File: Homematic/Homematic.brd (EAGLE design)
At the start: 99.2 x 85 mm, 26 parts, among them IC1 3.3V, IC2 3.3V, P1 DF11-06-2DS, Q1 BS170

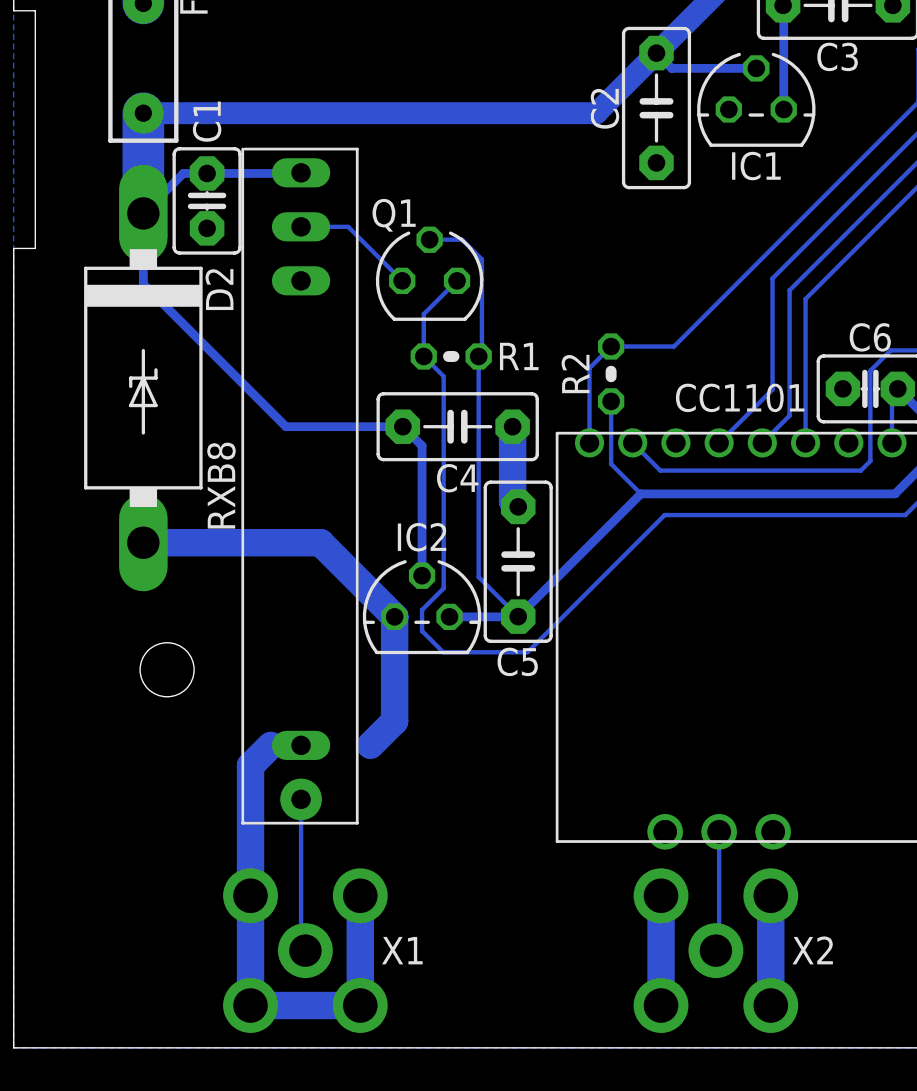
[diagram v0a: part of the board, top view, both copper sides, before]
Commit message: Fix RXB8 package. Add low pass filter.
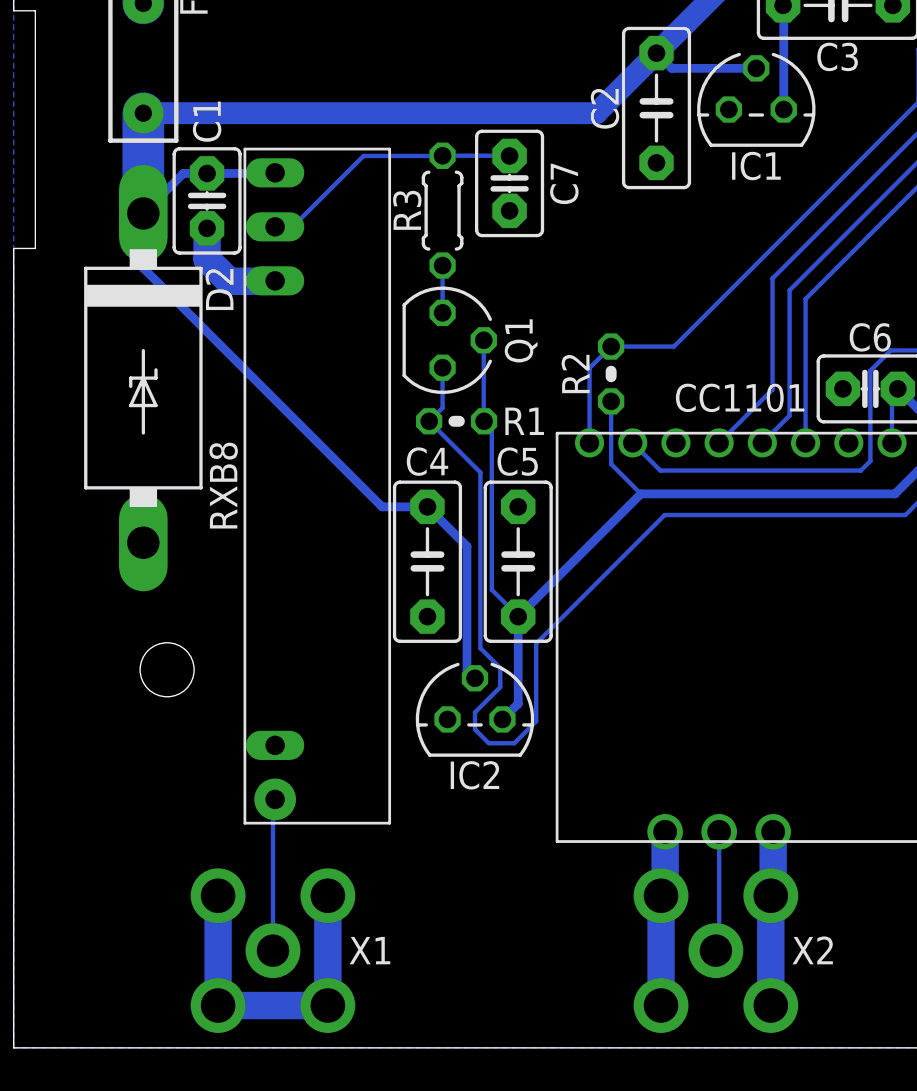
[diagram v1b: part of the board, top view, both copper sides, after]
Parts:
- added C7: 0.22uF, capacitor-wima:C2.5-3
- added R3: 100R, rcl:0204/5
- moved C4 6.40 mm to (19.1, 21.0), turned to 90 degrees
- moved IC2 5.34 mm to (21.4, 13.7)
- moved R1 3.01 mm to (20.5, 27.5)
- moved Q1 2.81 mm to (19.9, 31.2), turned to 270 degrees
- moved X1 1.50 mm to (12.0, 3.00)
- moved RXB8 1.20 mm to (12.1, 24.5)
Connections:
- new net N$11: Q1.D, R3.2
- net GND: now also C7.1
- net N$3: now also C7.2, R3.1; no longer Q1.D
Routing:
- net GND: track 73.5 -> 53.4 mm
- net N$3: track 5.72 -> 12.2 mm
- net +3V3: track 56.5 -> 51.7 mm
- net +5V: track 102.3 -> 104.9 mm
- net N$10: track 53.4 -> 55.9 mm
- net N$11: track 0.00 -> 2.19 mm

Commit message: Change low pass capacitor value from 220nF to 100nF.
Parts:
- C7: value 0.22uF -> 100nF
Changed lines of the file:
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@@
 <attribute name="VALUE" x="17.5386" y="39.3836" size="1.27" layer="27" ratio="10" rot="R270"/>
 </element>
-<element name="C7" library="capacitor-wima" package="C2.5-3" value="0.22uF" x="22.95" y="38.51" smashed="yes" rot="R90">
+<element name="C7" library="capacitor-wima" package="C2.5-3" value="100nF" x="22.95" y="38.51" smashed="yes" rot="R90">
 <attribute name="NAME" x="24.85" y="38.51" size="1.27" layer="25" font="vector" ratio="10" rot="R90" align="top-center"/>
 <attribute name="VALUE" x="25.998" y="36.859" size="1.27" layer="27" ratio="10" rot="R90"/>

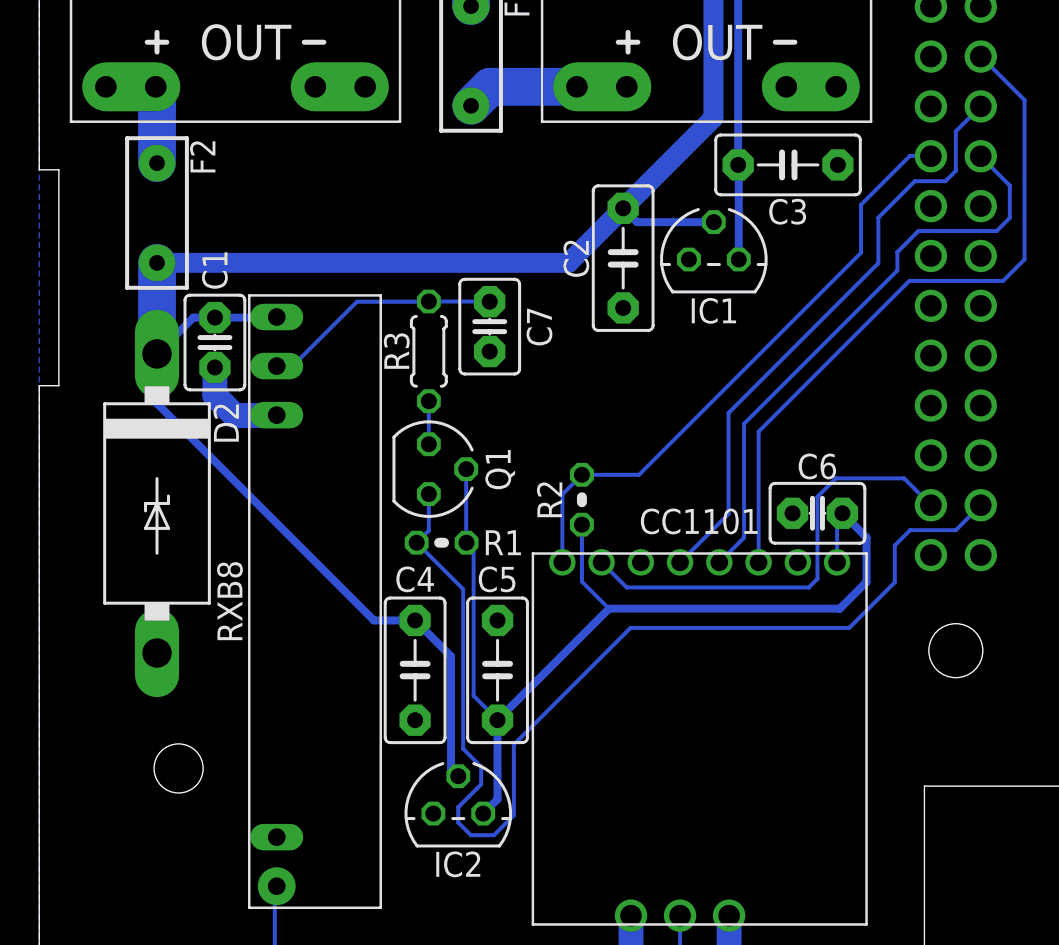
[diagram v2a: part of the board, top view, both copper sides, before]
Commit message: Fix low pass filter. Move suppressor diode. Move documentation from top to bottom layer.
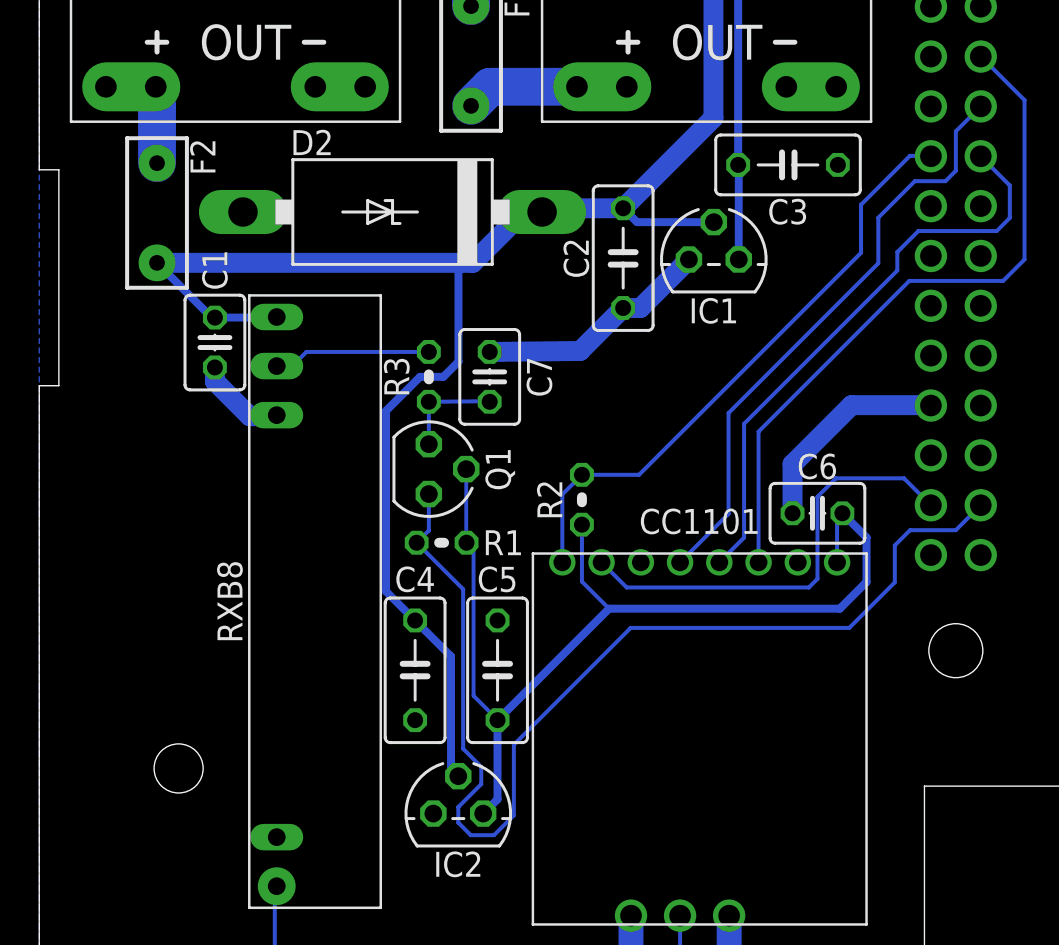
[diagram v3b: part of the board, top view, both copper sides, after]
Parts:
- R3: device rcl:0204/5 -> rcl:0204V
- moved D2 19.1 mm to (18.0, 44.4), turned to 180 degrees
- moved C7 2.56 mm to (22.9, 36.0), turned to 270 degrees
- moved R3 1.30 mm to (19.9, 36.0)
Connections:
- net N$11: now also C7.2
- net N$3: no longer C7.2
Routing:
- net GND: track 53.4 -> 75.9 mm
- net N$3: track 12.2 -> 8.07 mm
- net +5V: track 104.9 -> 101.5 mm
- net N$11: track 2.19 -> 5.29 mm

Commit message: Update design rules. Small changes of ground plane.
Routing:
- net GND: track 75.9 -> 0.00 mm
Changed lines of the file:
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@@
 <circle x="92.1" y="66" radius="3.1" width="0" layer="29"/>
 <text x="77" y="29" size="1.778" layer="52" ratio="10" rot="MR0">Homematic</text>
+<wire x1="22" y1="26.5" x2="22" y2="33.7" width="0.254" layer="42"/>
+<wire x1="10.9" y1="39.35" x2="10.9" y2="36.35" width="0.254" layer="42"/>
+<wire x1="47.27" y1="52.25" x2="47.27" y2="49.45" width="0.254" layer="42"/>
+<wire x1="48.675" y1="77.35" x2="48.675" y2="70.09" width="0.254" layer="42"/>
+<circle x="47.97" y="44.65" radius="0.5" width="0.4064" layer="42"/>
+<wire x1="47.95" y1="30.12" x2="45.15" y2="30.12" width="0.254" layer="42"/>
+<wire x1="47.53" y1="49.26" x2="45.93" y2="47.66" width="0.254" layer="42"/>
+<wire x1="47.49" y1="28.97" x2="45.89" y2="27.37" width="0.254" layer="42"/>
+<wire x1="44.75" y1="26.68" x2="43.15" y2="25.08" width="0.254" layer="42"/>
+<wire x1="27.03" y1="26.18" x2="28.63" y2="24.58" width="0.254" layer="42"/>
 </plain>
 <attributes>
@@
 <param name="mtIsolate" value="1.6mm 1.2mm 0.2mm 0.15mm 0.2mm 0.15mm 0.2mm 0.15mm 0.2mm 0.15mm 0.2mm 0.15mm 0.2mm 0.15mm 0.2mm"/>
 <param name="mdWireWire" value="6mil"/>
-<param name="mdWirePad" value="6mil"/>
+<param name="mdWirePad" value="8mil"/>
 <param name="mdWireVia" value="6mil"/>
-<param name="mdPadPad" value="6mil"/>
-<param name="mdPadVia" value="6mil"/>
-<param name="mdViaVia" value="8mil"/>
+<param name="mdPadPad" value="12mil"/>
+<param name="mdPadVia" value="8mil"/>
+<param name="mdViaVia" value="12mil"/>
 <param name="mdSmdPad" value="0mil"/>
 <param name="mdSmdVia" value="0mil"/>
@@
 <contactref element="C4" pad="1"/>
 <contactref element="C6" pad="2"/>
-<wire x1="15.85" y1="79.7" x2="20.83" y2="74.72" width="1.27" layer="16"/>
-<wire x1="20.83" y1="74.72" x2="22" y2="74.72" width="1.27" layer="16"/>
-<wire x1="16.604" y1="69.271" x2="22" y2="74.667" width="1.27" layer="16"/>
-<wire x1="22" y1="74.667" x2="22" y2="74.72" width="1.27" layer="16"/>
-<wire x1="40.604" y1="69.271" x2="41.383" y2="70.05" width="1.27" layer="16"/>
-<wire x1="29.96" y1="5.54" x2="29.96" y2="0.46" width="1.27" layer="16"/>
-<wire x1="35.04" y1="5.54" x2="35.04" y2="0.46" width="1.27" layer="16"/>
 <contactref element="CC1101" pad="GND0" route="any" routetag="G$1.GND"/>
 <contactref element="CC1101" pad="GND1" route="any" routetag="G$1.GND"/>
 <contactref element="CC1101" pad="GND2" route="any" routetag="G$1.GND"/>
-<wire x1="9.46" y1="5.54" x2="9.46" y2="0.46" width="1.27" layer="16"/>
-<wire x1="9.46" y1="0.46" x2="14.54" y2="0.46" width="1.27" layer="16"/>
-<wire x1="14.54" y1="5.54" x2="14.54" y2="0.46" width="1.27" layer="16"/>
 <contactref element="RXB8" pad="GND@1" route="any" routetag="G$1.GND"/>
 <contactref element="RXB8" pad="GND@2" route="any" routetag="G$1.GND"/>
@@
 <contactref element="RPI" pad="20" route="any" routetag="G$1.GND"/>
 <contactref element="RPI" pad="34" route="any" routetag="G$1.GND"/>
-<wire x1="30.15" y1="8.5" x2="30.15" y2="5.73" width="1.27" layer="16"/>
-<wire x1="30.15" y1="5.73" x2="29.96" y2="5.54" width="1.27" layer="16"/>
-<wire x1="35.15" y1="8.5" x2="35.15" y2="5.65" width="1.27" layer="16"/>
-<wire x1="35.15" y1="5.65" x2="35.04" y2="5.54" width="1.27" layer="16"/>
-<wire x1="8.95" y1="36.43" x2="8.95" y2="35.72" width="1.016" layer="16"/>
-<wire x1="8.95" y1="35.72" x2="10.72" y2="33.95" width="1.016" layer="16"/>
-<wire x1="10.72" y1="33.95" x2="12.05" y2="33.95" width="1.016" layer="16"/>
-<wire x1="12.05" y1="33.95" x2="12.1" y2="34" width="1.016" layer="16"/>
 <contactref element="C7" pad="1"/>
-<wire x1="22.95" y1="37.22" x2="27.56" y2="37.27" width="1.016" layer="16"/>
-<wire x1="27.56" y1="37.27" x2="29.75" y2="39.46" width="1.016" layer="16"/>
-<wire x1="29.75" y1="39.46" x2="30.63" y2="39.46" width="1.016" layer="16"/>
-<wire x1="30.63" y1="39.46" x2="33.1" y2="41.93" width="1.016" layer="16"/>
-<wire x1="38.38" y1="29" x2="38.38" y2="31.5" width="1.016" layer="16"/>
-<wire x1="38.38" y1="31.5" x2="41.39" y2="34.51" width="1.016" layer="16"/>
-<wire x1="41.39" y1="34.51" x2="45.41" y2="34.51" width="1.016" layer="16"/>
-<wire x1="45.41" y1="34.51" x2="45.43" y2="34.49" width="1.016" layer="16"/>
 </signal>
 <signal name="N$4">
@@
 <contactref element="C7" pad="2"/>
 <contactref element="Q1" pad="D"/>
-<wire x1="19.85" y1="34.68" x2="22.95" y2="34.71" width="0.2032" layer="16"/>
-<wire x1="22.95" y1="34.71" x2="22.95" y2="34.68" width="0.2032" layer="16"/>
 <wire x1="19.85" y1="32.52" x2="19.85" y2="34.68" width="0.2032" layer="16"/>
+<wire x1="19.85" y1="34.68" x2="22.95" y2="34.68" width="0.2032" layer="16"/>
 </signal>
 </signals>
